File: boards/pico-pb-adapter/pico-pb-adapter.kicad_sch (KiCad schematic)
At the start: 2 parts, among them U1 RPi_Pico, U2 PocketBeagle

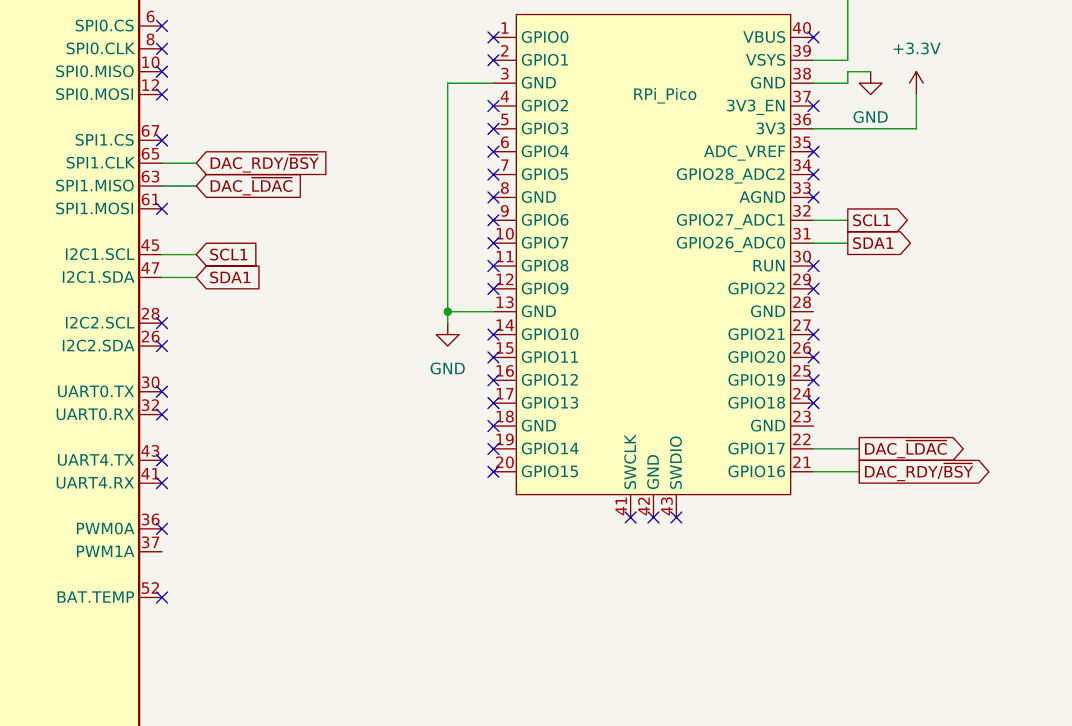
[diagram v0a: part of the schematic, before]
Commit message: compleded v1.0 adapter for raspberry pi pico to pocket-beagle socket (on solar sim controller board)
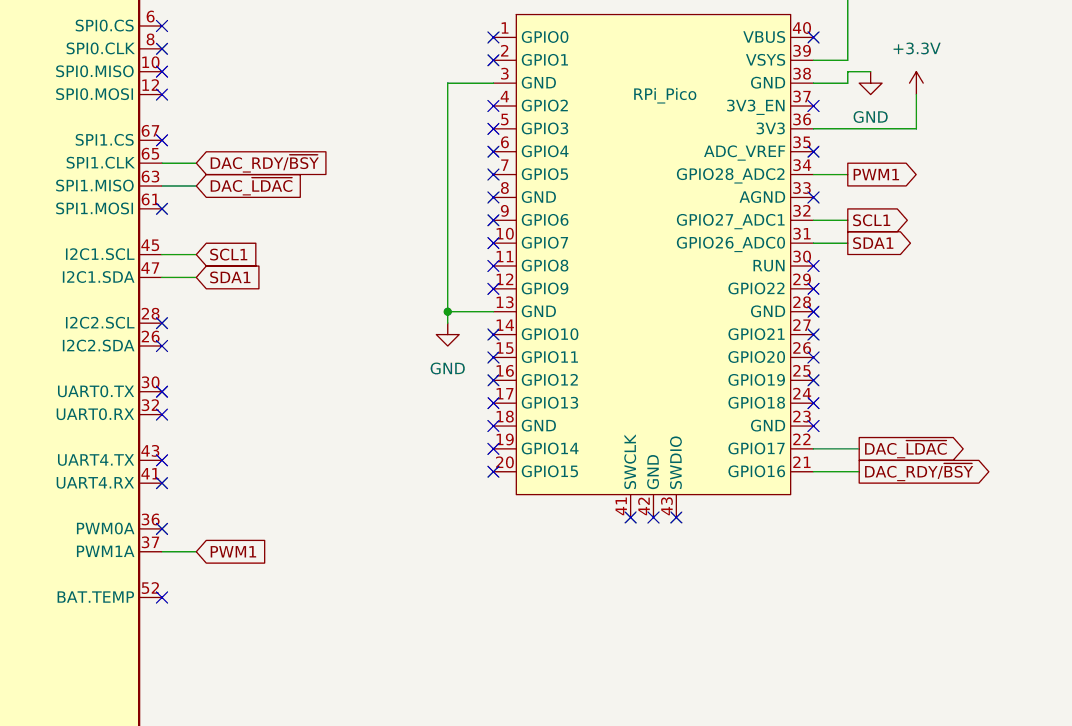
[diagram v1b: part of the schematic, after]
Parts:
- U1: symbol oresat-misc:Raspberry_Pi_Pico -> oresat-misc:RPi_Pico
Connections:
- net PWM1: now reaches U1.34 (GPIO28_ADC2)
- net PWM1: now also U2.37 (PWM1A)
- no-connect marks 91 -> 92
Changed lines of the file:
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@@
   (no_connect (at 109.22 110.49))
   (no_connect (at 146.05 101.6))
+  (no_connect (at 181.61 93.98))
   (no_connect (at 58.42 115.57))
   (no_connect (at 109.22 95.25))
@@
   (no_connect (at 146.05 99.06))
   (no_connect (at 99.06 36.83))
-  (no_connect (at 181.61 78.74))
   (no_connect (at 58.42 80.01))
   (no_connect (at 109.22 97.79))
@@
   (no_connect (at 146.05 109.22))
   (no_connect (at 161.29 116.84))
+  (no_connect (at 181.61 106.68))
   (no_connect (at 58.42 120.65))
   (no_connect (at 58.42 140.97))
@@
     (stroke (width 0) (type default))
   )
+  (wire (pts (xy 113.03 120.65) (xy 109.22 120.65))
+    (stroke (width 0) (type default))
+  )
   (wire (pts (xy 185.42 66.04) (xy 185.42 58.42))
     (stroke (width 0) (type default))
@@
     (stroke (width 0) (type default))
   )
+  (wire (pts (xy 140.97 93.98) (xy 140.97 95.25))
+    (stroke (width 0) (type default))
+  )
   (wire (pts (xy 181.61 73.66) (xy 193.04 73.66))
     (stroke (width 0) (type default))
@@
     (stroke (width 0) (type default))
   )
+  (wire (pts (xy 140.97 93.98) (xy 146.05 93.98))
+    (stroke (width 0) (type default))
+  )
   (wire (pts (xy 113.03 87.63) (xy 109.22 87.63))
     (stroke (width 0) (type default))
@@
     (stroke (width 0) (type default))
   )
-  (wire (pts (xy 140.97 93.98) (xy 146.05 93.98))
+  (wire (pts (xy 185.42 78.74) (xy 181.61 78.74))
     (stroke (width 0) (type default))
   )
@@
     (stroke (width 0) (type default))
   )
-  (wire (pts (xy 140.97 95.25) (xy 140.97 93.98))
-    (stroke (width 0) (type default))
-  )
   (wire (pts (xy 140.97 68.58) (xy 140.97 93.98))
     (stroke (width 0) (type default))
@@
     (effects (font (size 1.27 1.27)) (justify left))
     (property "Intersheetrefs" "${INTERSHEET_REFS}" (at 120.7928 90.17 0)
+      (effects (font (size 1.27 1.27)) (justify left) hide)
+    )
+  )
+  (global_label "PWM1" (shape output) (at 185.42 78.74 0) (fields_autoplaced)
+    (effects (font (size 1.27 1.27)) (justify left))
+    (property "Intersheetrefs" "${INTERSHEET_REFS}" (at 193.7875 78.74 0)
+      (effects (font (size 1.27 1.27)) (justify left) hide)
+    )
+  )
+  (global_label "PWM1" (shape input) (at 113.03 120.65 0) (fields_autoplaced)
+    (effects (font (size 1.27 1.27)) (justify left))
+    (property "Intersheetrefs" "${INTERSHEET_REFS}" (at 121.3975 120.65 0)
       (effects (font (size 1.27 1.27)) (justify left) hide)
     )
@@
     )
   )
-  (symbol (lib_id "oresat-misc:Raspberry_Pi_Pico") (at 162.56 87.63 0) (unit 1)
+  (symbol (lib_id "oresat-misc:RPi_Pico") (at 162.56 87.63 0) (unit 1)
     (in_bom yes) (on_board yes) (dnp no) (fields_autoplaced)
     (property "Reference" "U1" (at 163.83 58.42 0)

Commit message: Small changes for production, maybe? And upgraded to KiCAD 8.
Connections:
- net GND: now also U1.18 (GND), U1.23 (GND), U1.28 (GND), U1.33 (AGND), U1.42 (GND)
- no-connect marks 92 -> 87
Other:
- note added: "From external supply"
- note added: "Generated by Pico"
- note added: "Input from SS"
- note added: "Output to SS"
- title: (none) -> PB to Pico Adapter Board for Solar Simulator
- moved on the sheet: U1, U2
